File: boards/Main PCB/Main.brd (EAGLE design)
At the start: 101.6 x 76.2 mm, 115 parts, among them CN1 MINIB, CN2 MINIB, IC1 FT232RL, IC2 FT232RL, IC4 OKR-T_3-W12-C, J1 3_PIN_JST-XH, J2 2_PIN_JST-XH, J3 5_PIN_JST-XH, Q4 BSS138, Q5 BSS138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

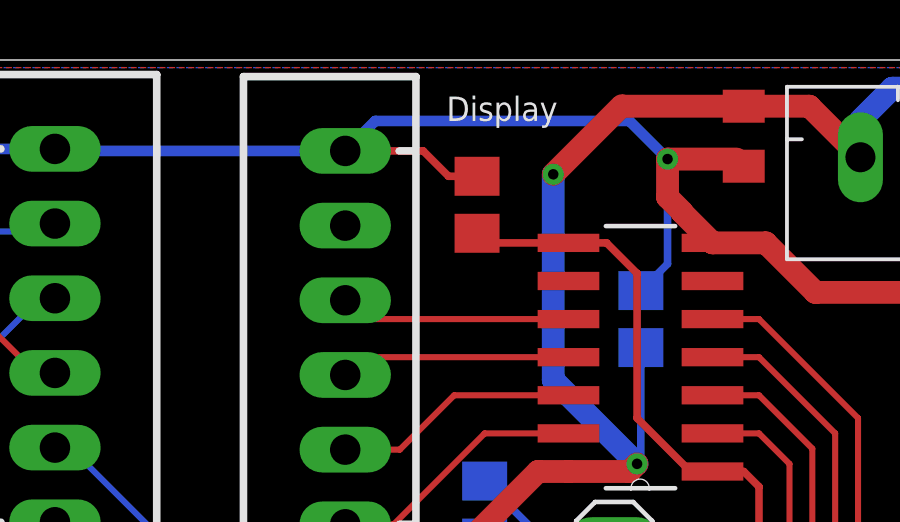
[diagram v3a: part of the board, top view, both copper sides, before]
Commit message: Connecting 5V line for display IC
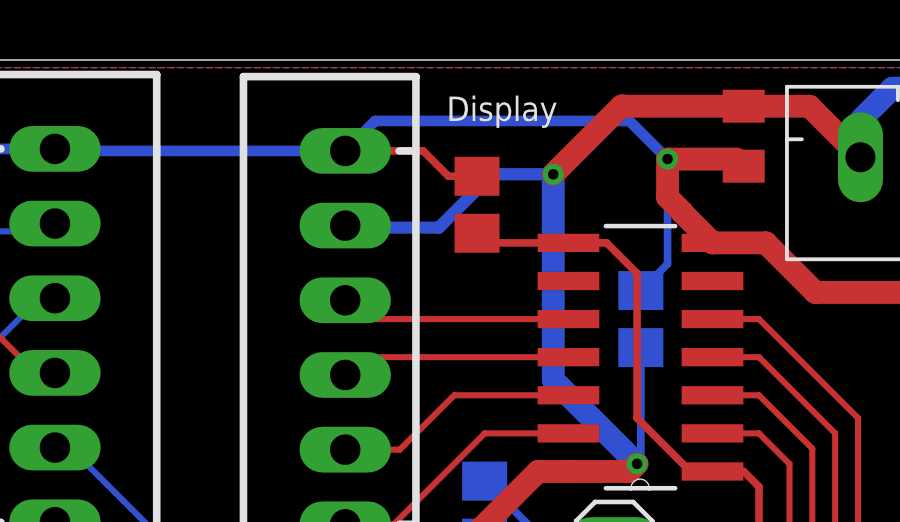
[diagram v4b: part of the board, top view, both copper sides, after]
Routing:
- net +5V: track 166.7 -> 173.6 mm
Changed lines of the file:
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@@
 <?xml version="1.0" encoding="utf-8"?>
 <!DOCTYPE eagle SYSTEM "eagle.dtd">
-<eagle version="9.2.2">
+<eagle version="9.3.1">
 <drawing>
 <settings>
@@
 <wire x1="54.102" y1="62.738" x2="53.848" y2="62.484" width="0.762" layer="1"/>
 <wire x1="53.848" y1="62.484" x2="51.816" y2="62.484" width="0.762" layer="1"/>
-<wire x1="44.9498" y1="70.104" x2="44.374" y2="70.6798" width="0.254" layer="1"/>
 <wire x1="26.416" y1="24.262" x2="26.416" y2="34.544" width="0.762" layer="1"/>
 <contactref element="R33" pad="2"/>
@@
 <via x="51.308" y="72.39" extent="1-16" drill="0.35"/>
 <wire x1="51.308" y1="72.39" x2="53.594" y2="74.676" width="0.762" layer="1"/>
-<wire x1="51.308" y1="65.532" x2="44.9498" y2="70.104" width="0" layer="19" extent="1-16"/>
+<wire x1="51.308" y1="72.39" x2="49.276" y2="72.39" width="0.4064" layer="16"/>
+<wire x1="49.276" y1="72.39" x2="47.498" y2="70.612" width="0.4064" layer="16"/>
+<wire x1="47.498" y1="70.612" x2="44.4418" y2="70.612" width="0.4064" layer="16"/>
+<wire x1="44.4418" y1="70.612" x2="44.374" y2="70.6798" width="0.3048" layer="16"/>
 </signal>
 <signal name="N$5">

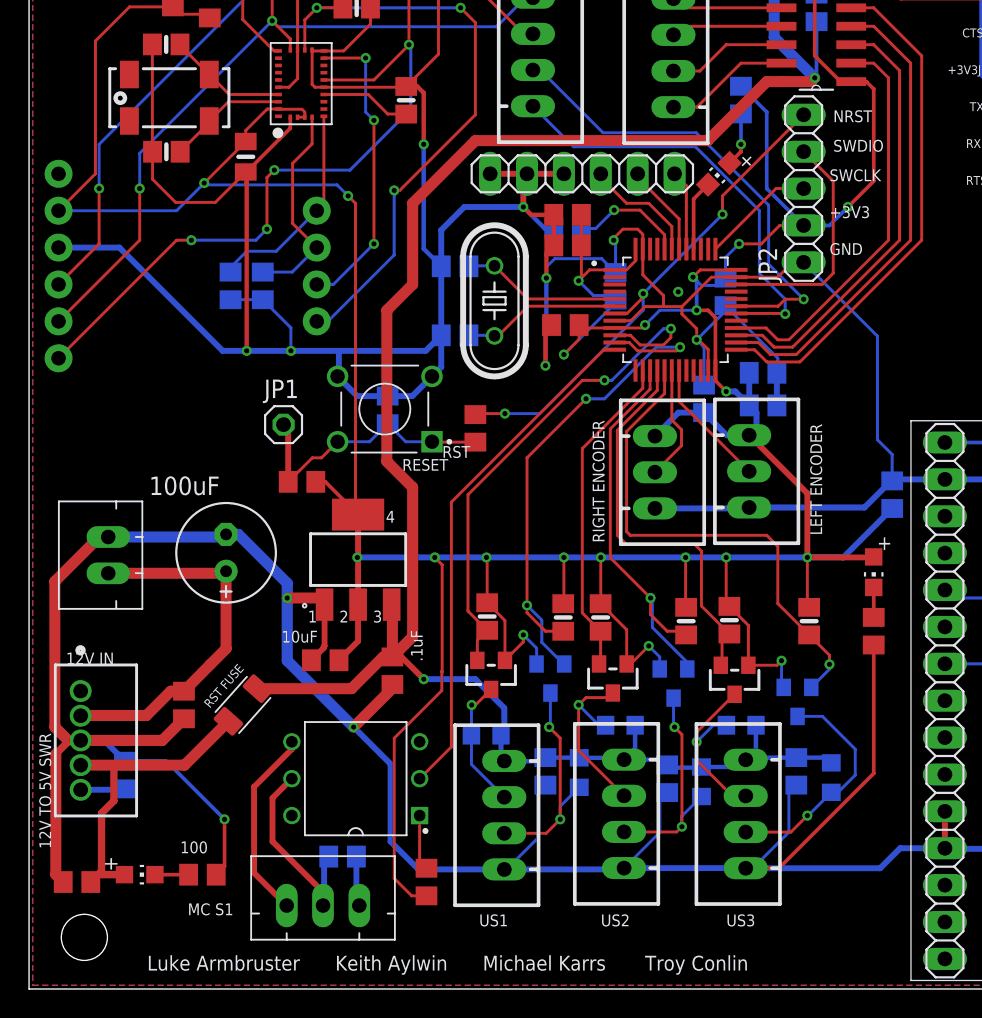
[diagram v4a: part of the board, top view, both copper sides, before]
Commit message: Moving some traces for final design
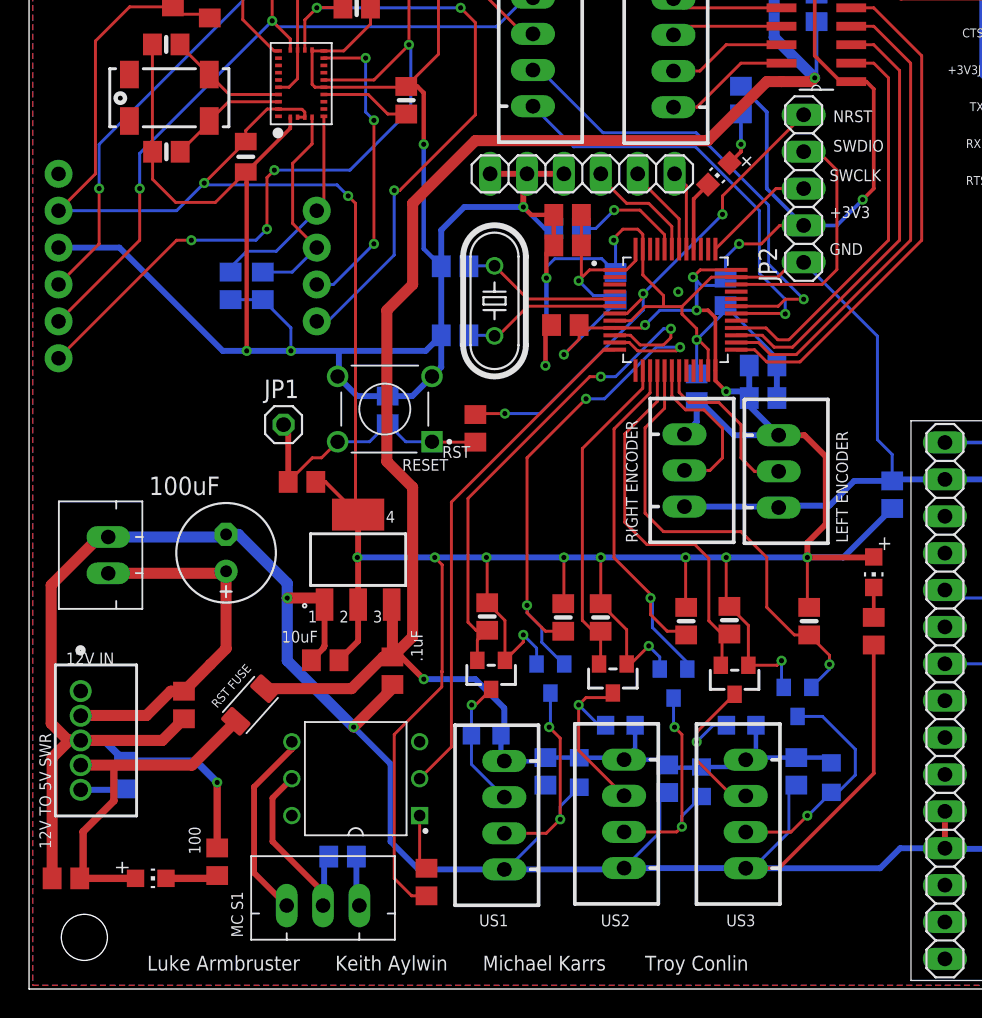
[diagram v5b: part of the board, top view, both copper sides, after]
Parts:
- moved X6 2.04 mm to (45.1, 35.7)
- moved X7 2.03 mm to (51.6, 35.6)
- moved R32 1.35 mm to (13.0, 8.76), turned to 270 degrees
- moved C29 0.92 mm to (46.0, 41.4)
- moved C31 0.80 mm to (2.54, 7.62)
- moved RX4 0.80 mm to (8.38, 7.62)
- moved C16 0.51 mm to (50.5, 42.9)
- moved R33 0.51 mm to (15.2, 19.6)
- moved C23 0.51 mm to (50.5, 40.7)
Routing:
- net GND: track 769.2 -> 764.5 mm
- net +3V3: track 323.2 -> 326.9 mm
- net ADC_CH8: track 8.04 -> 11.2 mm
- net ADC_CH9: track 8.94 -> 11.9 mm
- net US3_ECHO: track 34.7 -> 31.9 mm
- net N$21: track 24.8 -> 26.7 mm
- net N$12: track 2.32 -> 3.60 mm
- net US3_TRIG: track 27.6 -> 26.7 mm
- net SWDIO: track 16.2 -> 17.0 mm
- net +5V: track 173.6 -> 173.1 mm

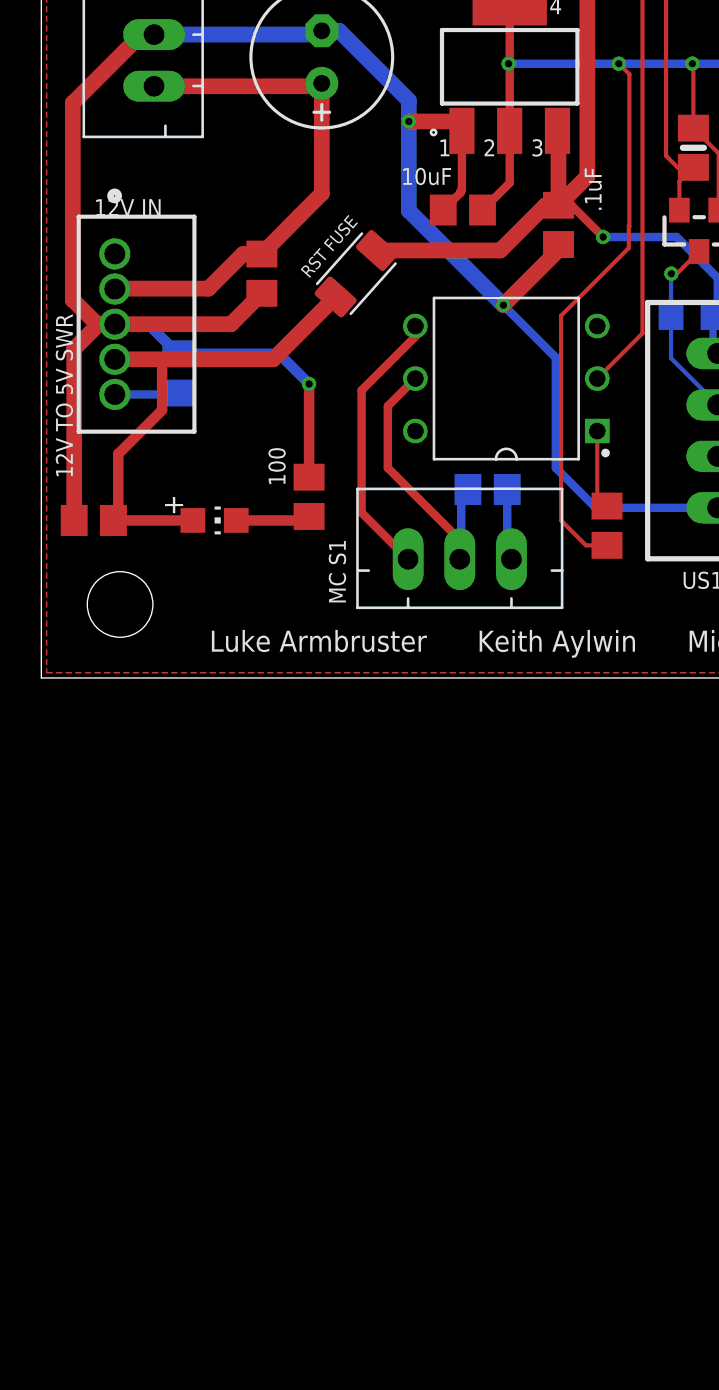
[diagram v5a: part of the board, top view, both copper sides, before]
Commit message: Added a TL431 and Thyristor
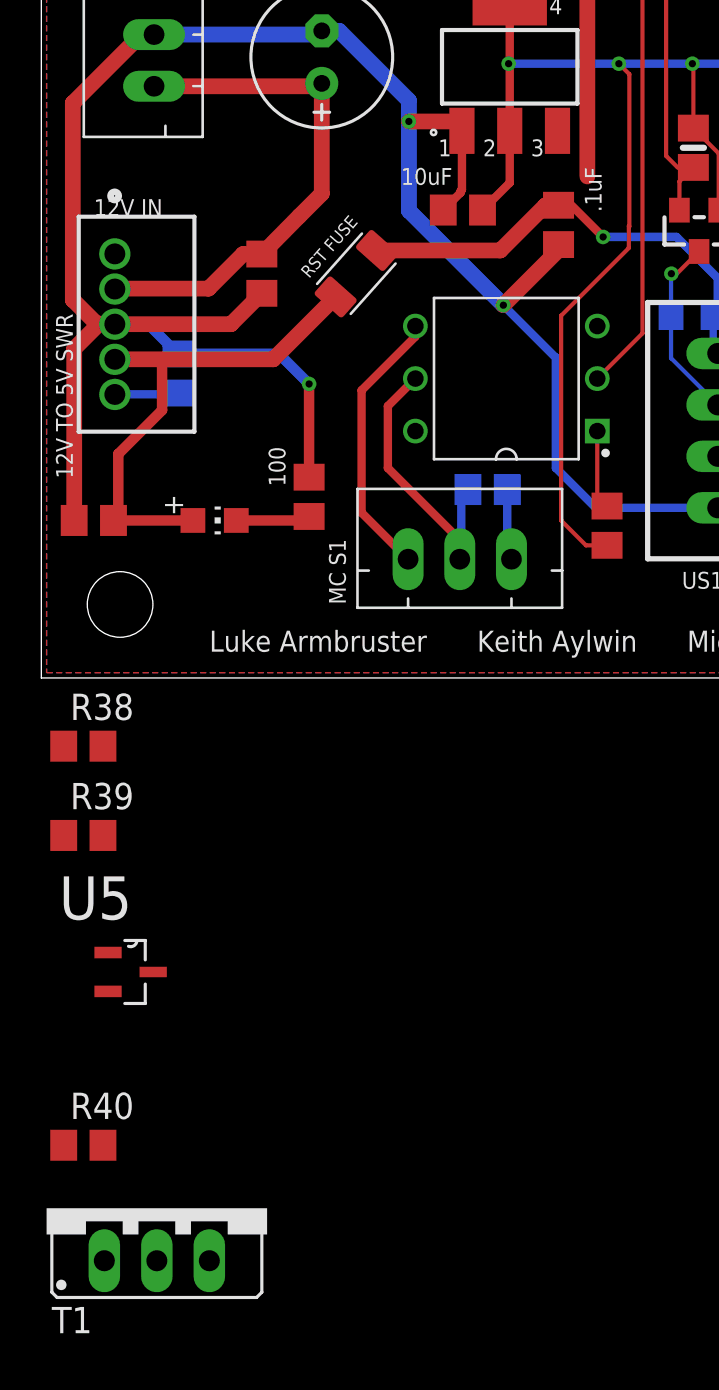
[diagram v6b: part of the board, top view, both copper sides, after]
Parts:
- added R38, R39: (no value), resistor:R0805
- added R40: 10k, resistor:R0805
- added T1: TIC116, triac:TO220CS
- added U5: TL431AIDBZTG4, main_library:SOT95P237X112-3N
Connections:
- new net N$25: R38.1, R39.2, U5.2
- new net N$30: R40.2, T1.G, U5.3
- net +5V: now also R38.2, T1.A, U5.1
- net GND: now also R39.1, R40.1, T1.C
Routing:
- net +5V: track 173.1 -> 167.0 mm
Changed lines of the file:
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@@
 <?xml version="1.0" encoding="utf-8"?>
 <!DOCTYPE eagle SYSTEM "eagle.dtd">
-<eagle version="9.2.2">
+<eagle version="9.3.1">
 <drawing>
 <settings>
@@
 <attribute name="SPICEPREFIX" value="C" x="48.768" y="71.374" size="1.778" layer="27" rot="R90" display="off"/>
 <attribute name="VALUE" x="49.53" y="69.088" size="0.6096" layer="27" rot="R180"/>
+</element>
+<element name="R38" library="resistor" library_urn="urn:adsk.eagle:library:348" package="R0805" package3d_urn="urn:adsk.eagle:package:26059/1" value="" x="2.032" y="-3.302" smashed="yes">
+<attribute name="NAME" x="1.397" y="-2.032" size="1.27" layer="25"/>
+<attribute name="VALUE" x="1.397" y="-5.842" size="1.27" layer="27"/>
+</element>
+<element name="R39" library="resistor" library_urn="urn:adsk.eagle:library:348" package="R0805" package3d_urn="urn:adsk.eagle:package:26059/1" value="" x="2.032" y="-7.62" smashed="yes">
+<attribute name="NAME" x="1.397" y="-6.35" size="1.27" layer="25"/>
+<attribute name="VALUE" x="1.397" y="-10.16" size="1.27" layer="27"/>
+</element>
+<element name="U5" library="main_library" package="SOT95P237X112-3N" value="TL431AIDBZTG4" x="4.318" y="-14.224" smashed="yes">
+<attribute name="AVAILABILITY" value="Unavailable" x="4.318" y="-14.224" size="1.778" layer="27" display="off"/>
+<attribute name="DESCRIPTION" value=" V-Ref Adjustable 2.495V to 36V 100mA Automotive 3-Pin SOT-23 T/R " x="4.318" y="-14.224" size="1.778" layer="27" display="off"/>
+<attribute name="MF" value="Texas Instruments" x="4.318" y="-14.224" size="1.778" layer="27" display="off"/>
+<attribute name="MP" value="TL431AIDBZTG4" x="4.318" y="-14.224" size="1.778" layer="27" display="off"/>
+<attribute name="NAME" x="0.863190625" y="-11.683690625" size="2.08305" layer="25" ratio="10" rot="SR0"/>
+<attribute name="PACKAGE" value="SOT-23-3 Texas Instruments" x="4.318" y="-14.224" size="1.778" layer="27" display="off"/>
+<attribute name="PRICE" value="None" x="4.318" y="-14.224" size="1.778" layer="27" display="off"/>
+<attribute name="VALUE" x="0.859490625" y="-18.674290625" size="2.08528125" layer="27" ratio="10" rot="SR0"/>
+</element>
+<element name="R40" library="resistor" library_urn="urn:adsk.eagle:library:348" package="R0805" package3d_urn="urn:adsk.eagle:package:26059/1" value="10k" x="2.032" y="-22.606" smashed="yes">
+<attribute name="NAME" x="1.397" y="-21.336" size="1.27" layer="25"/>
+<attribute name="VALUE" x="1.397" y="-25.146" size="1.27" layer="27"/>
+</element>
+<element name="T1" library="triac" library_urn="urn:adsk.eagle:library:403" package="TO220CS" package3d_urn="urn:adsk.eagle:package:30140/2" value="TIC116" x="5.588" y="-25.654" smashed="yes">
+<attribute name="NAME" x="0.508" y="-31.6992" size="1.27" layer="25" ratio="10"/>
+<attribute name="VALUE" x="0.508" y="-33.274" size="1.27" layer="27" ratio="10"/>
 </element>
 </elements>
@@
 <wire x1="47.818" y1="72.324" x2="46.973" y2="73.169" width="0.254" layer="1"/>
 <wire x1="12.954" y1="9.713" x2="12.954" y2="14.224" width="0.508" layer="1"/>
+<contactref element="R39" pad="1"/>
+<contactref element="R40" pad="1"/>
+<contactref element="T1" pad="C"/>
+<wire x1="1.082" y1="-22.606" x2="3.048" y2="-28.194" width="0" layer="19" extent="1-1"/>
+<wire x1="1.082" y1="-7.62" x2="1.082" y2="-22.606" width="0" layer="19" extent="1-1"/>
+<wire x1="1.59" y1="7.62" x2="1.082" y2="-7.62" width="0" layer="19" extent="1-1"/>
 </signal>
 <signal name="D+_GPS">
@@
 <wire x1="53.848" y1="62.484" x2="51.816" y2="62.484" width="0.762" layer="1"/>
 <wire x1="26.416" y1="24.262" x2="26.416" y2="34.544" width="0.762" layer="1"/>
-<contactref element="R33" pad="2"/>
-<contactref element="C8" pad="1"/>
-<contactref element="U1" pad="3"/>
 <wire x1="26.416" y1="48.514" x2="26.416" y2="54.102" width="0.762" layer="1"/>
-<wire x1="16.24116875" y1="20.6816875" x2="22.2056875" y2="20.6816875" width="0.762" layer="1"/>
-<wire x1="24.392" y1="22.868" x2="25.022" y2="22.868" width="0.762" layer="1"/>
-<wire x1="22.2056875" y1="20.6816875" x2="24.392" y2="22.868" width="0.762" layer="1"/>
-<wire x1="25.022" y1="22.868" x2="25.022" y2="26.4186" width="0.762" layer="1"/>
-<wire x1="25.022" y1="26.4186" x2="24.9714" y2="26.4692" width="0.508" layer="1"/>
-<wire x1="25.022" y1="22.868" x2="26.416" y2="24.262" width="0.762" layer="1"/>
-<wire x1="25.022" y1="22.868" x2="25.646" y2="22.868" width="0.4064" layer="1"/>
 <wire x1="25.646" y1="22.868" x2="27.178" y2="21.336" width="0.4064" layer="1"/>
 <contactref element="C18" pad="1"/>
@@
 <wire x1="47.498" y1="70.612" x2="44.4418" y2="70.612" width="0.4064" layer="16"/>
 <wire x1="44.4418" y1="70.612" x2="44.374" y2="70.6798" width="0.3048" layer="16"/>
+<contactref element="U1" pad="3"/>
+<wire x1="25.022" y1="26.4186" x2="24.9714" y2="26.4692" width="0.508" layer="1"/>
+<contactref element="R33" pad="2"/>
+<contactref element="C8" pad="1"/>
+<contactref element="R38" pad="2"/>
+<contactref element="U5" pad="1"/>
+<contactref element="T1" pad="A"/>
+<wire x1="16.24116875" y1="20.6816875" x2="22.2056875" y2="20.6816875" width="0.762" layer="1"/>
+<wire x1="24.392" y1="22.868" x2="25.022" y2="22.868" width="0.762" layer="1"/>
+<wire x1="22.2056875" y1="20.6816875" x2="24.392" y2="22.868" width="0.762" layer="1"/>
+<wire x1="25.646" y1="22.868" x2="26.416" y2="24.262" width="0" layer="19" extent="1-1"/>
+<wire x1="25.022" y1="22.868" x2="25.646" y2="22.868" width="0" layer="19" extent="1-1"/>
+<wire x1="25.022" y1="26.4186" x2="26.416" y2="24.262" width="0" layer="19" extent="1-1"/>
+<wire x1="2.982" y1="-3.302" x2="16.24116875" y2="20.6816875" width="0" layer="19" extent="1-1"/>
+<wire x1="3.2258" y1="-13.2842" x2="2.982" y2="-3.302" width="0" layer="19" extent="1-1"/>
+<wire x1="5.588" y1="-28.194" x2="3.2258" y2="-13.2842" width="0" layer="19" extent="1-1"/>
 </signal>
 <signal name="N$5">
@@
 <via x="44.704" y="48.006" extent="1-16" drill="0.35"/>
 </signal>
+<signal name="N$25">
+<contactref element="R38" pad="1"/>
+<contactref element="R39" pad="2"/>
+<contactref element="U5" pad="2"/>
+<wire x1="2.982" y1="-7.62" x2="3.2258" y2="-15.1638" width="0" layer="19" extent="1-1"/>
+<wire x1="1.082" y1="-3.302" x2="2.982" y2="-7.62" width="0" layer="19" extent="1-1"/>
+</signal>
+<signal name="N$30">
+<contactref element="U5" pad="3"/>
+<contactref element="R40" pad="2"/>
+<contactref element="T1" pad="G"/>
+<wire x1="2.982" y1="-22.606" x2="8.128" y2="-28.194" width="0" layer="19" extent="1-1"/>
+<wire x1="5.4102" y1="-14.224" x2="2.982" y2="-22.606" width="0" layer="19" extent="1-1"/>
+</signal>
 </signals>
